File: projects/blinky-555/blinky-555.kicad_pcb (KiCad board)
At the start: 2 copper layers, 70 x 45 mm, 13 parts, among them J1 9-12V IN, U1 NE555P

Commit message: fix(MD-T8): place decoupling caps at their IC supply pins (blinky C3, reflex C13)
Co-Authored-By: Claude Opus 5.5 <noreply@anthropic.com>
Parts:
- moved C3 22.1 mm to (136.0, 67.5)
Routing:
- net /OUT: track 24.2 -> 28.9 mm
- net /VCC: track 54.8 -> 57.8 mm
- net GND: vias 159 -> 162

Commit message: fix(MD-T11): derive via/stitch spacing from fab rules (no flaky hole_to_hole)
Co-Authored-By: Claude Opus 5.5 <noreply@anthropic.com>
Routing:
- net GND: vias 162 -> 165

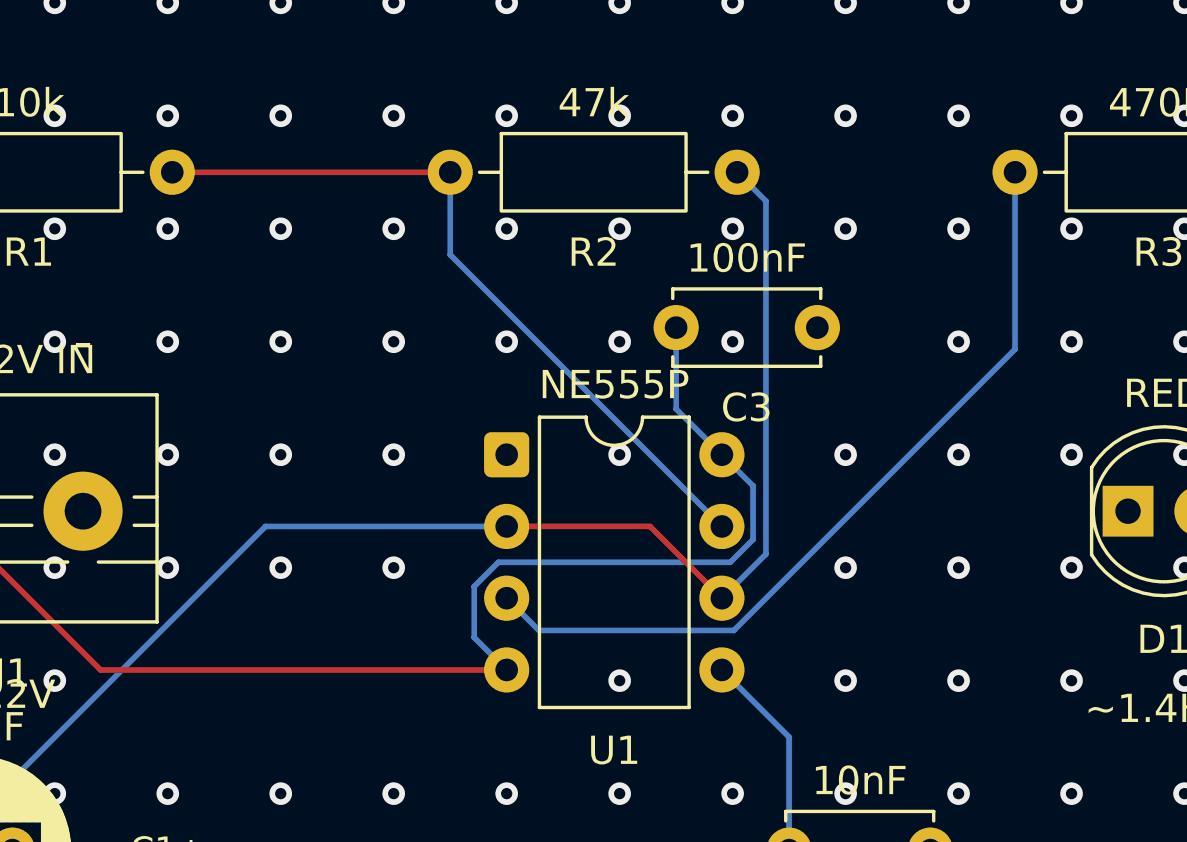
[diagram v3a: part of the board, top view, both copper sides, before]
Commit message: fix(P1-T9b): keep LCSC ids, package family match, PR-BYNAME
Co-Authored-By: Claude Opus 5.5 <noreply@anthropic.com>
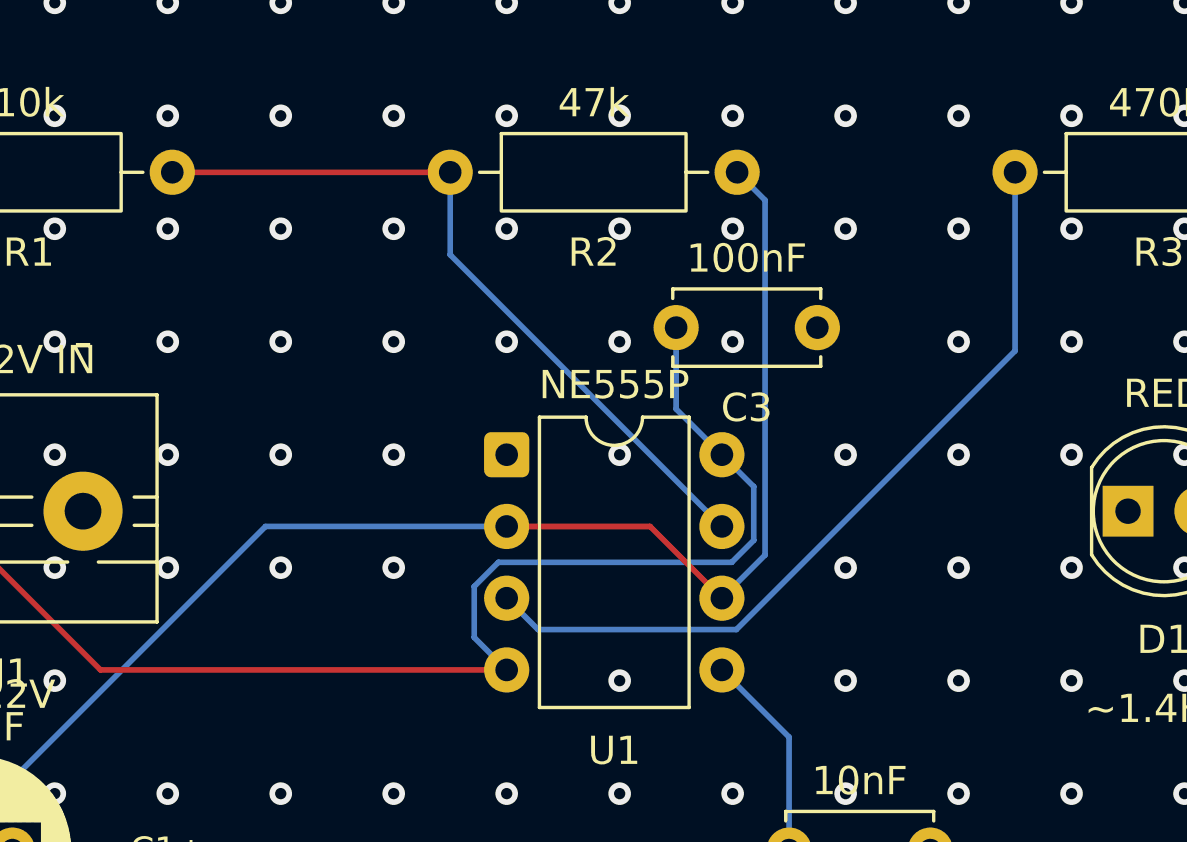
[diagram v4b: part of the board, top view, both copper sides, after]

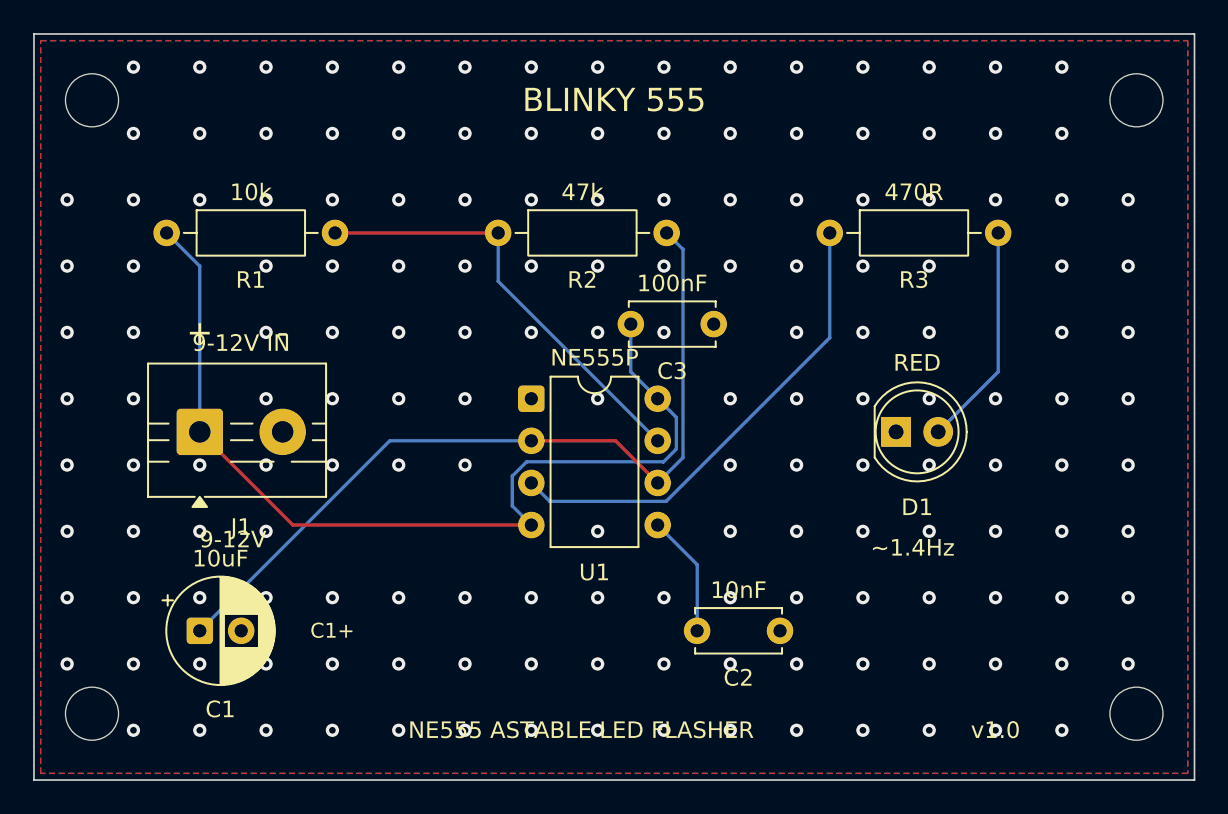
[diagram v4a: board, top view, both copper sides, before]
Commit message: feat(P2-T7b): RC-filter recognition, direction severities, expansion class; blinky reverse-polarity diode
Co-Authored-By: Claude Opus 5.5 <noreply@anthropic.com>
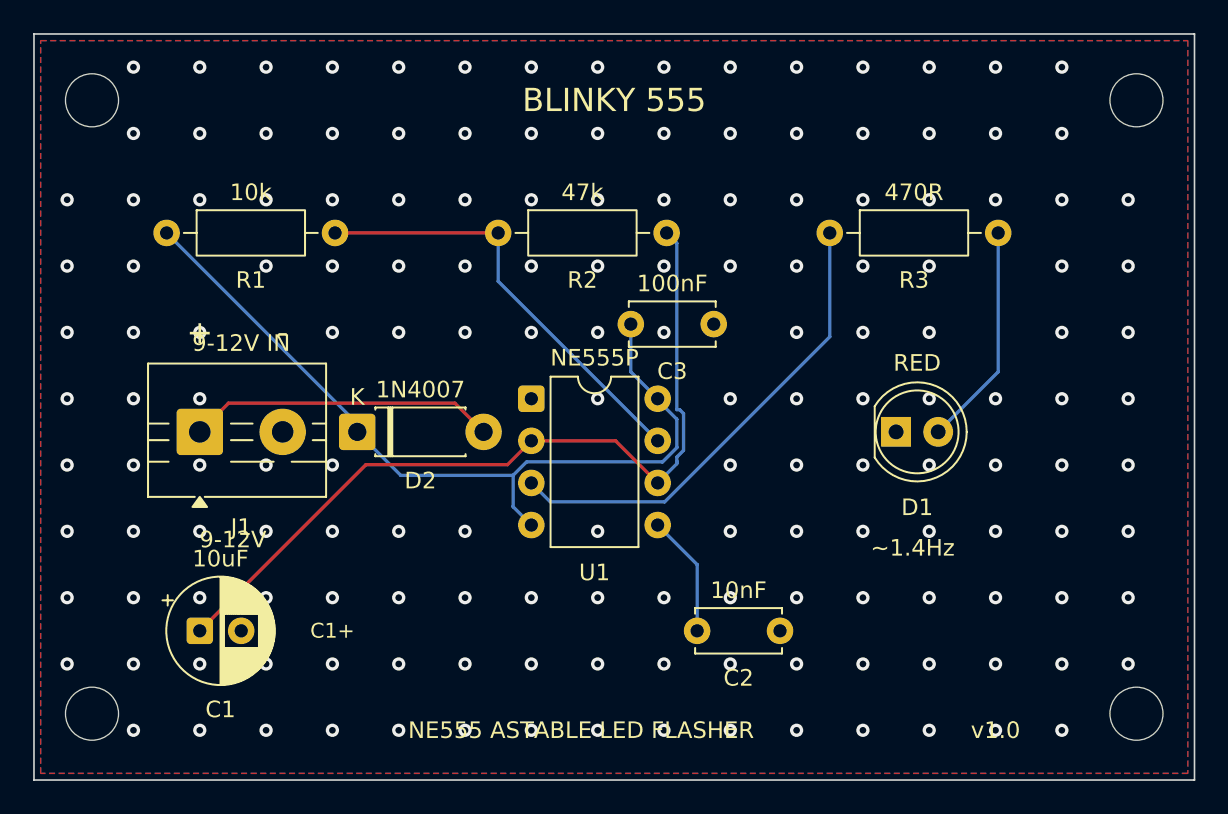
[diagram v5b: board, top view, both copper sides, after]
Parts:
- added D2: 1N4007, Diode_THT:D_DO-41_SOD81_P7.62mm_Horizontal, F.Cu at (119.5, 74.0)
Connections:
- J1 pad 1: /VCC -> /VIN
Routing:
- net /VIN: track 0.00 -> 18.6 mm
- net /VCC: track 57.8 -> 49.9 mm
- net GND: vias 165 -> 163
